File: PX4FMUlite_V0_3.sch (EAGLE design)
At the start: 155 parts, among them J2 DF13-4P-1.25V, J201 DF13C-6P-1.25V, J202 DF13C-6P-1.25V, J203 DF13C-6P-1.25V, J3 DF13C-4P-1.25V, J302 DF13C-4P-1.25V, J401 DF13C-4P-1.25V, J403 DF13C-7P-1.25V, J405 DF13C-4P-1.25V, J801 JST-ZH-3, J802 DF13C-3P-1.25V, M3_MOUNT1101 MOUNT-HOLE3.1MM, M3_MOUNT1102 MOUNT-HOLE3.1MM, M3_MOUNT1103 MOUNT-HOLE3.1MM, M3_MOUNT1104 MOUNT-HOLE3.1MM, U101 STM32F4X7VX, U2 MAX3051, U401 MAX3051, U903 74LVC2G240, X101 3.2x2.5 mm / 24 MHz / 15 ppm

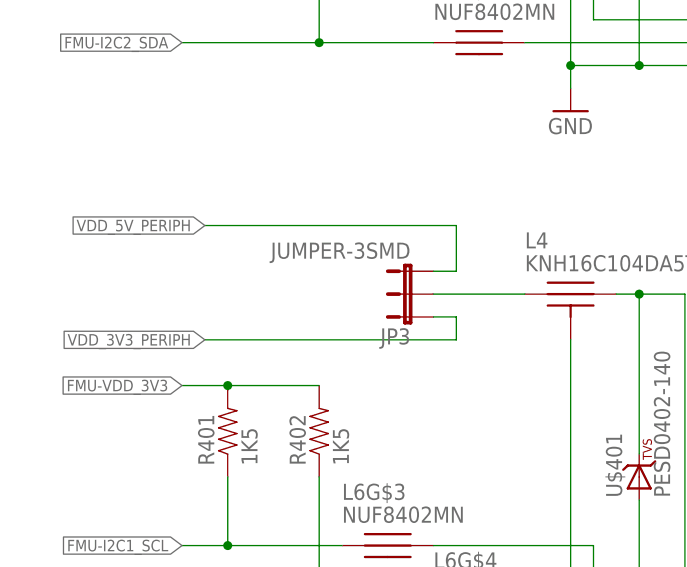
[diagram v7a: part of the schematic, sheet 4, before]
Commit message: started to wire MAX21100
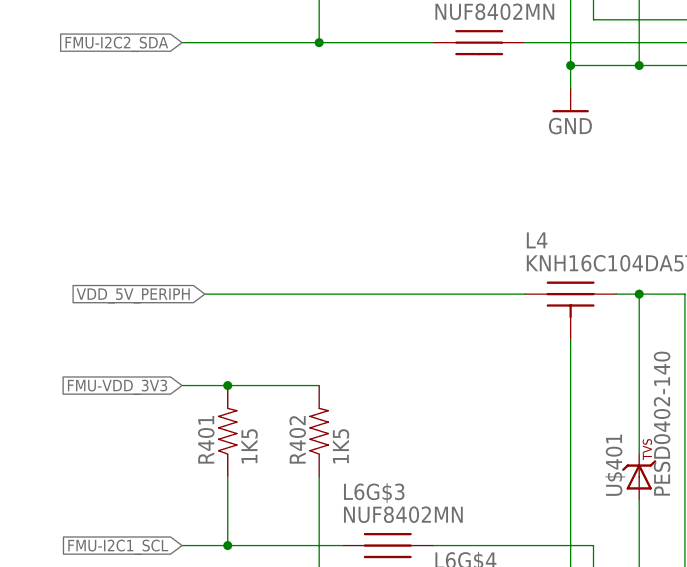
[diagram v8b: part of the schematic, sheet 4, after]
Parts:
- removed JP3: JUMPER-3SMD, SparkFun-Passives:JUMPER-3SMD
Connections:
- removed net N$31: JP3.2, L4.P$1
- net VDD_3V3_PERIPH: no longer JP3.1
- net VDD_5V_PERIPH: now also L4.P$1; no longer JP3.3
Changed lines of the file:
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@@
 </part>
 <part name="SJ2" library="SparkFun-Passives" deviceset="SOLDERJUMPER" device="TRACE"/>
-<part name="JP3" library="SparkFun-Passives" deviceset="JUMPER-3" device="SMD"/>
 <part name="U$2" library="PX4lite" deviceset="MAX21100" device=""/>
 <part name="C5" library="pixhawk2" deviceset="CAP" device="0402" value="0u1">
@@
 </instance>
 <instance part="SJ2" gate="1" x="205.74" y="106.68"/>
-<instance part="JP3" gate="G$1" x="53.34" y="50.8" rot="R90"/>
 </instances>
 <busses>
@@
 </segment>
 </net>
-<net name="N$31" class="1">
-<segment>
-<pinref part="L4" gate="G$1" pin="P$1"/>
-<pinref part="JP3" gate="G$1" pin="2"/>
-<wire x1="55.88" y1="53.34" x2="66.04" y2="53.34" width="0.1524" layer="91"/>
-</segment>
-</net>
 <net name="CAN2_TX" class="0">
 <segment>
@@
 </segment>
 </net>
-<net name="VDD_3V3_PERIPH" class="1">
-<segment>
-<label x="30.48" y="48.26" size="1.27" layer="95" rot="R180" xref="yes"/>
-<wire x1="58.42" y1="48.26" x2="30.48" y2="48.26" width="0.1524" layer="91"/>
-<pinref part="JP3" gate="G$1" pin="1"/>
-<wire x1="55.88" y1="50.8" x2="58.42" y2="50.8" width="0.1524" layer="91"/>
-<wire x1="58.42" y1="50.8" x2="58.42" y2="48.26" width="0.1524" layer="91"/>
-</segment>
-</net>
 <net name="VDD_5V_PERIPH" class="1">
 <segment>
@@
 </segment>
 <segment>
-<label x="30.48" y="60.96" size="1.27" layer="95" rot="R180" xref="yes"/>
-<wire x1="58.42" y1="60.96" x2="30.48" y2="60.96" width="0.1524" layer="91"/>
-<pinref part="JP3" gate="G$1" pin="3"/>
-<wire x1="55.88" y1="55.88" x2="58.42" y2="55.88" width="0.1524" layer="91"/>
-<wire x1="58.42" y1="55.88" x2="58.42" y2="60.96" width="0.1524" layer="91"/>
+<label x="30.48" y="53.34" size="1.27" layer="95" rot="R180" xref="yes"/>
+<wire x1="66.04" y1="53.34" x2="30.48" y2="53.34" width="0.1524" layer="91"/>
+<pinref part="L4" gate="G$1" pin="P$1"/>
 </segment>
 <segment>
@@
 </segment>
 </net>
-<net name="VDD_3V3_PERIPH" class="1">
-<segment>
-<wire x1="48.26" y1="48.26" x2="38.1" y2="48.26" width="0.1524" layer="91"/>
-<label x="33.02" y="48.26" size="1.27" layer="95" rot="MR0" xref="yes"/>
-<pinref part="U903" gate="G$1" pin="VCC"/>
-<pinref part="C901" gate="G$1" pin="1"/>
-<wire x1="38.1" y1="48.26" x2="33.02" y2="48.26" width="0.1524" layer="91"/>
-<wire x1="38.1" y1="38.1" x2="38.1" y2="48.26" width="0.1524" layer="91"/>
-<junction x="38.1" y="48.26"/>
-</segment>
-</net>
 <net name="RSSI_IN" class="0">
 <segment>
@@
 </segment>
 </net>
+<net name="VDD_3V3_PERIPH" class="1">
+<segment>
+<wire x1="48.26" y1="48.26" x2="38.1" y2="48.26" width="0.1524" layer="91"/>
+<label x="33.02" y="48.26" size="1.27" layer="95" rot="MR0" xref="yes"/>
+<pinref part="U903" gate="G$1" pin="VCC"/>
+<pinref part="C901" gate="G$1" pin="1"/>
+<wire x1="38.1" y1="48.26" x2="33.02" y2="48.26" width="0.1524" layer="91"/>
+<wire x1="38.1" y1="38.1" x2="38.1" y2="48.26" width="0.1524" layer="91"/>
+<junction x="38.1" y="48.26"/>
+</segment>
+</net>
